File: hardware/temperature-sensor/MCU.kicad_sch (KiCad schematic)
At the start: 4 parts, among them U1 STM32F407V_E-G_Tx, Y1 CX2016FB25000C0FZZH1

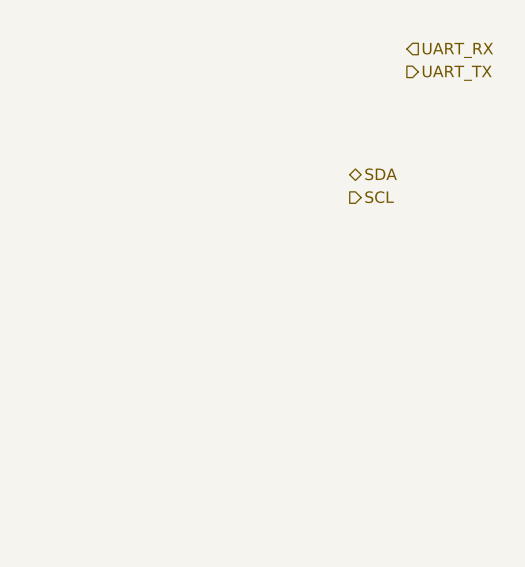
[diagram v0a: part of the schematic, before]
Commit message: add connection to FAN PWM and TACH
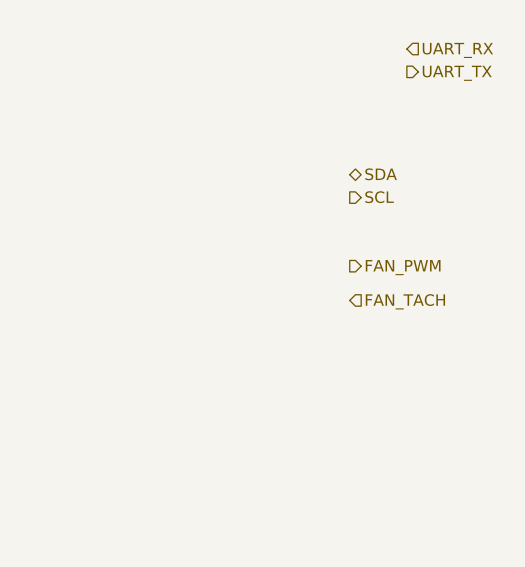
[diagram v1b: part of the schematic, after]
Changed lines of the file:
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@@
+		)
+	)
+	(hierarchical_label "FAN_PWM"
+		(shape output)
+		(at 224.79 114.3 0)
+		(effects
+			(font
+				(size 1.27 1.27)
+			)
+			(justify left)
 		)
 	)
@@
 		)
 	)
+	(hierarchical_label "FAN_TACH"
+		(shape input)
+		(at 224.79 118.11 0)
+		(effects
+			(font
+				(size 1.27 1.27)
+			)
+			(justify left)
+		)
+	)

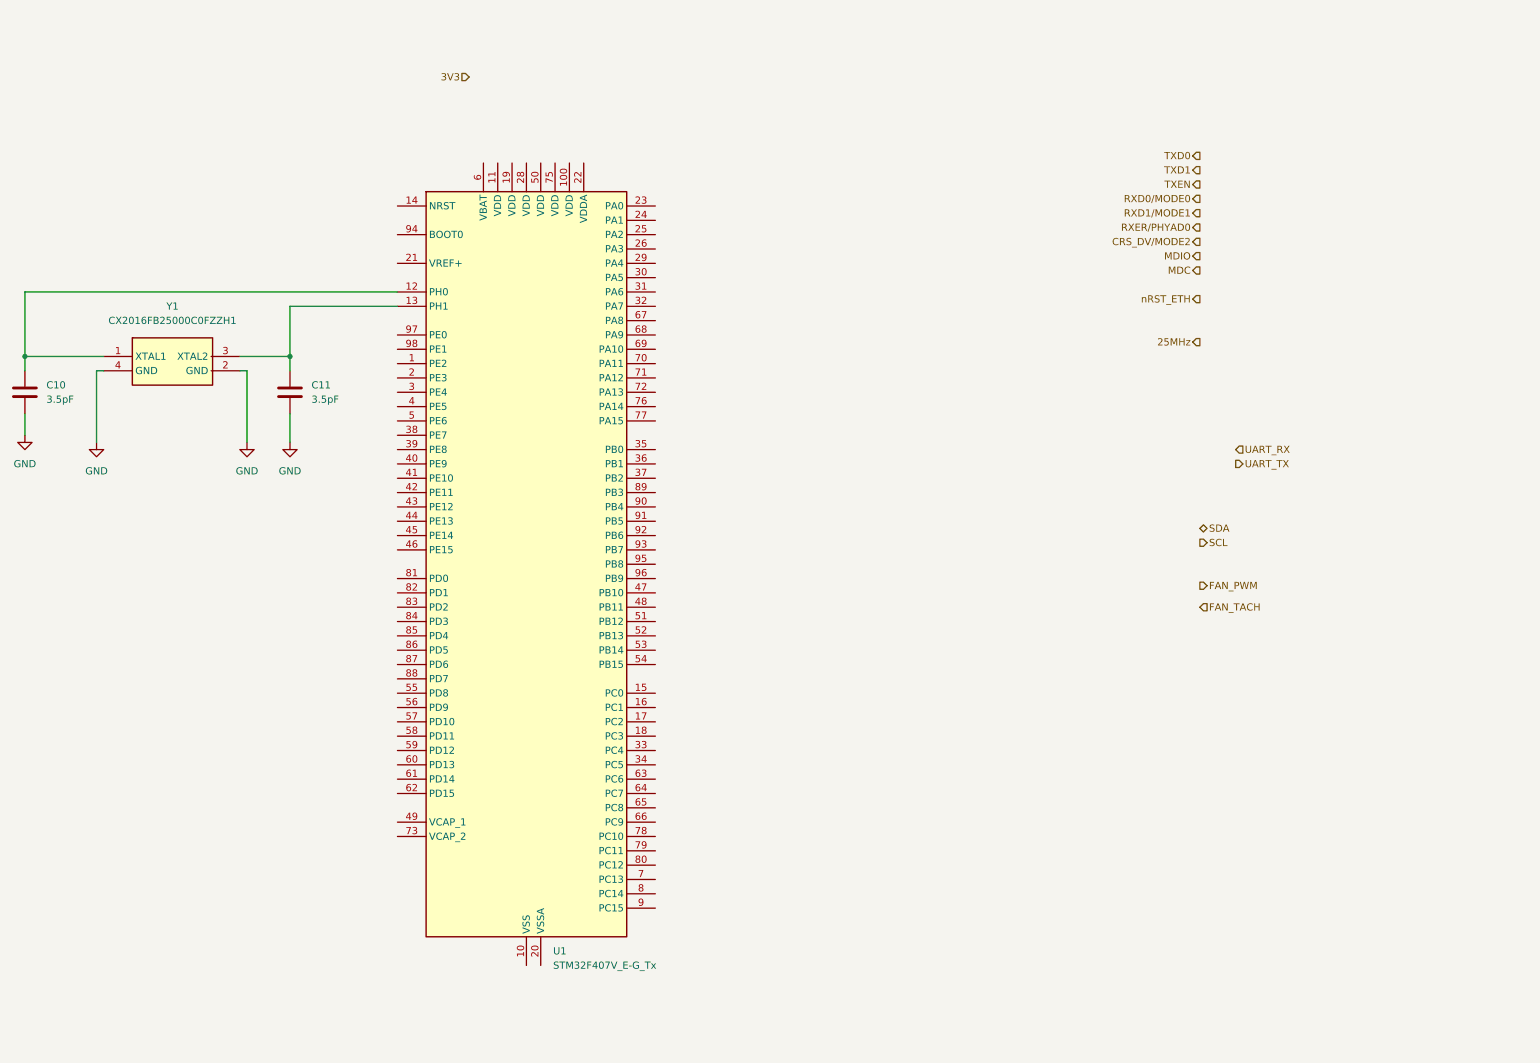
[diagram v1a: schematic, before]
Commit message: work on temperature sensor
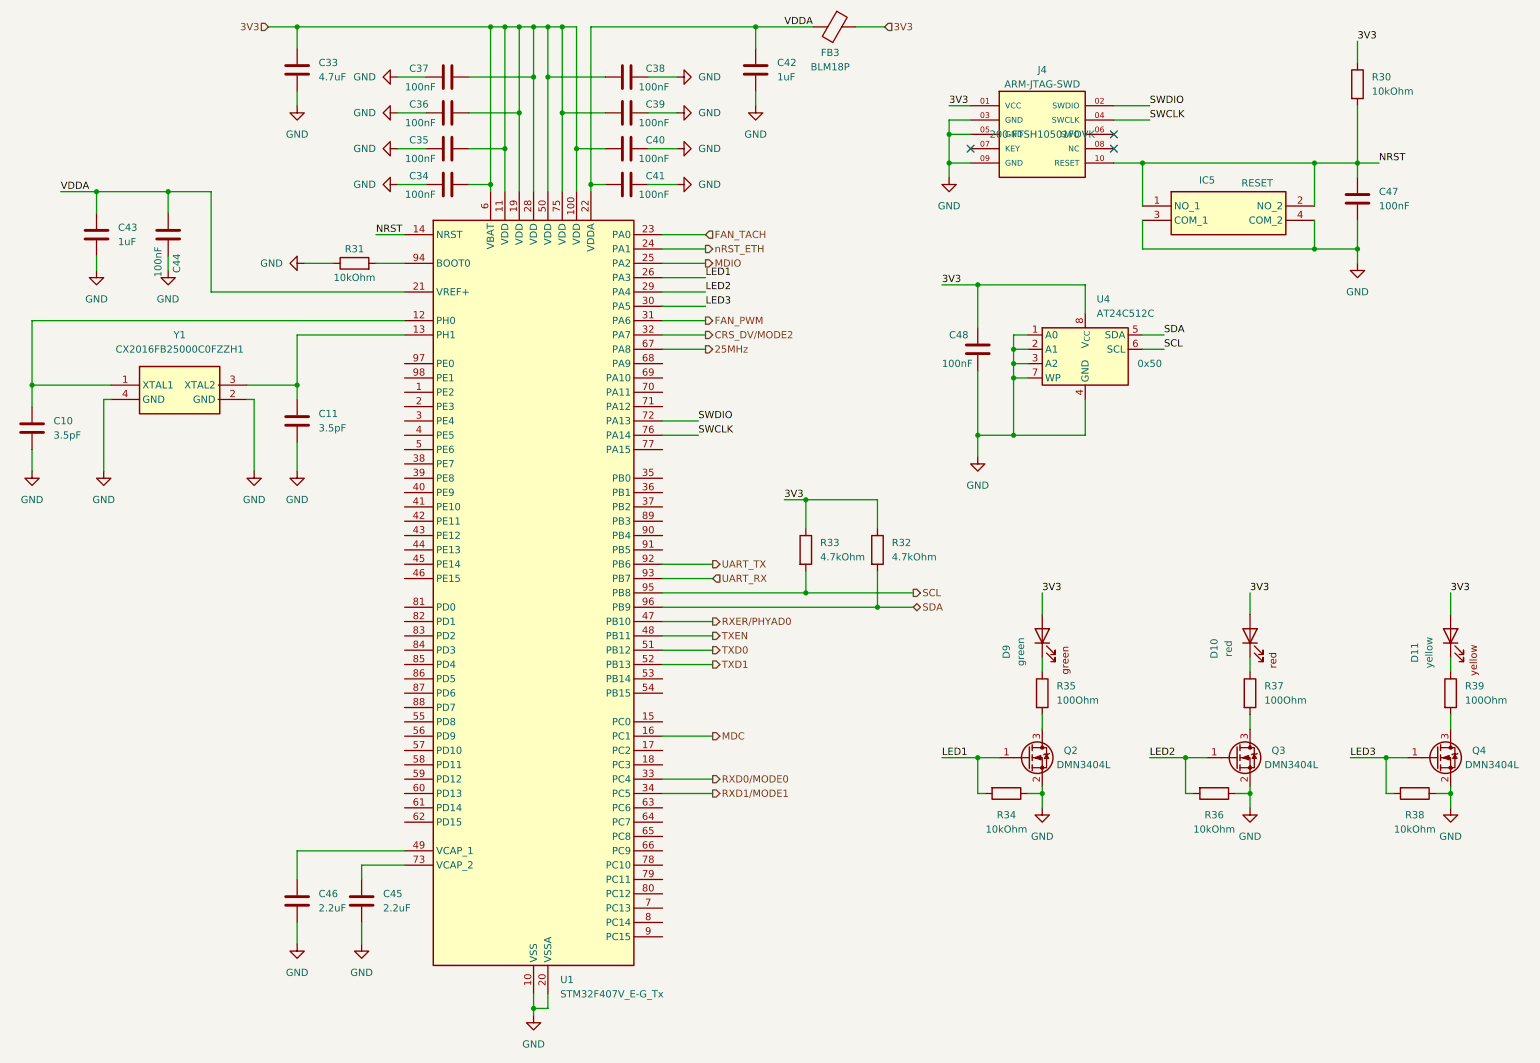
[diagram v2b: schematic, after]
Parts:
- added C33: 4.7uF, benediktibk:C_0805_2012Metric_Pad1.18x1.45mm_HandSolder, symbol benediktibk:C_4_7uF_SMD_0805_50V_10%
- added C34, C35, C36, C37, C38, C39, C40, C41, C44, C47, C48: 100nF, benediktibk:C_0603_1608Metric_Pad1.08x0.95mm_HandSolder, symbol benediktibk:C_100nF_SMD_0603_50V
- added C42, C43: 1uF, benediktibk:C_0603_1608Metric_Pad1.08x0.95mm_HandSolder, symbol benediktibk:C_1uF_SMD_0603_50V_10%
- added C45, C46: 2.2uF, benediktibk:C_0603_1608Metric_Pad1.08x0.95mm_HandSolder, symbol benediktibk:C_2_2uF_SMD_0603_10V_10%
- added D10: red, benediktibk:D_0603_1608Metric_Pad1.05x0.95mm_HandSolder, symbol benediktibk:LED_red_0603
- added D11: yellow, benediktibk:D_0603_1608Metric_Pad1.05x0.95mm_HandSolder, symbol benediktibk:LED_yellow_0603
- added D9: green, benediktibk:D_0603_1608Metric_Pad1.05x0.95mm_HandSolder, symbol benediktibk:LED_green_0603
- added FB3: BLM18P, benediktibk:R_0603_1608Metric_Pad0.98x0.95mm_HandSolder, symbol benediktibk:BLM18P
- added IC5: RESET, benediktibk:TS026650BK100SCRD, symbol benediktibk:TS02-66-50-BK-100-SCR-D
- added J4: ARM-JTAG-SWD, benediktibk:SAMTEC_FTSH-105-01-F-DV-P-TR, symbol benediktibk:ARM-JTAG-SWD
- added Q2, Q3, Q4: DMN3404L, benediktibk:SOT-23, symbol benediktibk:DMN3404L
- added R30, R31, R34, R36, R38: 10kOhm, benediktibk:R_0603_1608Metric_Pad0.98x0.95mm_HandSolder, symbol benediktibk:R_10kOhm_SMD_0603_100mW_1%
- added R32, R33: 4.7kOhm, benediktibk:R_0603_1608Metric_Pad0.98x0.95mm_HandSolder, symbol benediktibk:R_4_7kOhm_SMD_0603_100mW_1%
- added R35, R37, R39: 100Ohm, benediktibk:R_0603_1608Metric_Pad0.98x0.95mm_HandSolder, symbol benediktibk:R_100Ohm_SMD_0603_100mW_1%
- added U4: AT24C512C, benediktibk:SOIC127P600X175-8N, symbol benediktibk:AT24C512C
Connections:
- net 25MHz: now also U1.67 (PA8)
- net 3V3: now also U1.100 (VDD), U1.11 (VDD), U1.19 (VDD), U1.28 (VDD), U1.50 (VDD), U1.6 (VBAT), U1.75 (VDD), C33.1, C34.1, C35.1, C36.1, C37.1, C38.1, C39.1, C40.1, C48.1, D10.2 (A), D11.2 (A), D9.2 (A), FB3.1, J4.01 (VCC), R30.1, R32.1, R33.1, U4.8 (V_{CC})
- net CRS_DV/MODE2: now also U1.32 (PA7)
- net FAN_PWM: now also U1.31 (PA6)
- net FAN_TACH: now also U1.23 (PA0)
- net GND: now also U1.10 (VSS), U1.20 (VSSA), U1.27 (VSS), U1.74 (VSS), U1.99 (VSS), C33.2, C34.2, C35.2, C36.2, C37.2, C38.2, C39.2, C40.2, C41.2, C42.2, C43.2, C44.2, C45.2, C46.2, C47.2, C48.2, IC5.3 (COM_1), IC5.4 (COM_2), J4.03 (GND), J4.05 (GND), J4.09 (GND), Q2.2 (S), Q3.2 (S), Q4.2 (S), R31.1, R34.1, R36.1, R38.1, U4.1 (A0), U4.2 (A1), U4.3 (A2), U4.4 (GND), U4.7 (WP)
- net MDC: now also U1.16 (PC1)
- net MDIO: now also U1.25 (PA2)
- net RXD0/MODE0: now also U1.33 (PC4)
- net RXD1/MODE1: now also U1.34 (PC5)
- net RXER/PHYAD0: now also U1.47 (PB10)
- net SCL: now also U1.95 (PB8), R33.2, U4.6 (SCL)
- net SDA: now also U1.96 (PB9), R32.2, U4.5 (SDA)
- net TXD0: now also U1.51 (PB12)
- net TXD1: now also U1.52 (PB13)
- net TXEN: now also U1.48 (PB11)
- net UART_RX: now also U1.93 (PB7)
- net UART_TX: now also U1.92 (PB6)
- net nRST_ETH: now also U1.24 (PA1)
- net NRST: now reaches U1.14 (NRST)
- net NRST: now also C47.1, IC5.1 (NO_1), IC5.2 (NO_2), J4.10 (RESET), R30.2
- net VDDA: now reaches U1.21 (VREF+)
- net VDDA: now also U1.22 (VDDA), C41.1, C42.1, C43.1, C44.1, FB3.2
- net LED1: now reaches U1.26 (PA3)
- net LED1: now also Q2.1 (G), R34.2
- net LED2: now reaches U1.29 (PA4)
- net LED2: now also Q3.1 (G), R36.2
- net LED3: now reaches U1.30 (PA5)
- net LED3: now also Q4.1 (G), R38.2
- net at U1.49 (VCAP_1): now also C46.1
- net SWDIO: now reaches U1.72 (PA13)
- net SWDIO: now also J4.02 (SWDIO)
- net at U1.73 (VCAP_2): now also C45.1
- net SWCLK: now reaches U1.76 (PA14)
- net SWCLK: now also J4.04 (SWCLK)
- net at U1.94 (BOOT0): now also R31.2
- new net: D10.1 (K), R37.1
- new net: Q3.3 (D), R37.2
- new net: D11.1 (K), R39.1
- new net: Q2.3 (D), R35.2
- new net: Q4.3 (D), R39.2
- new net: D9.1 (K), R35.1
- no-connect marks 0 -> 3
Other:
- moved on the sheet: C10, C11, U1, Y1

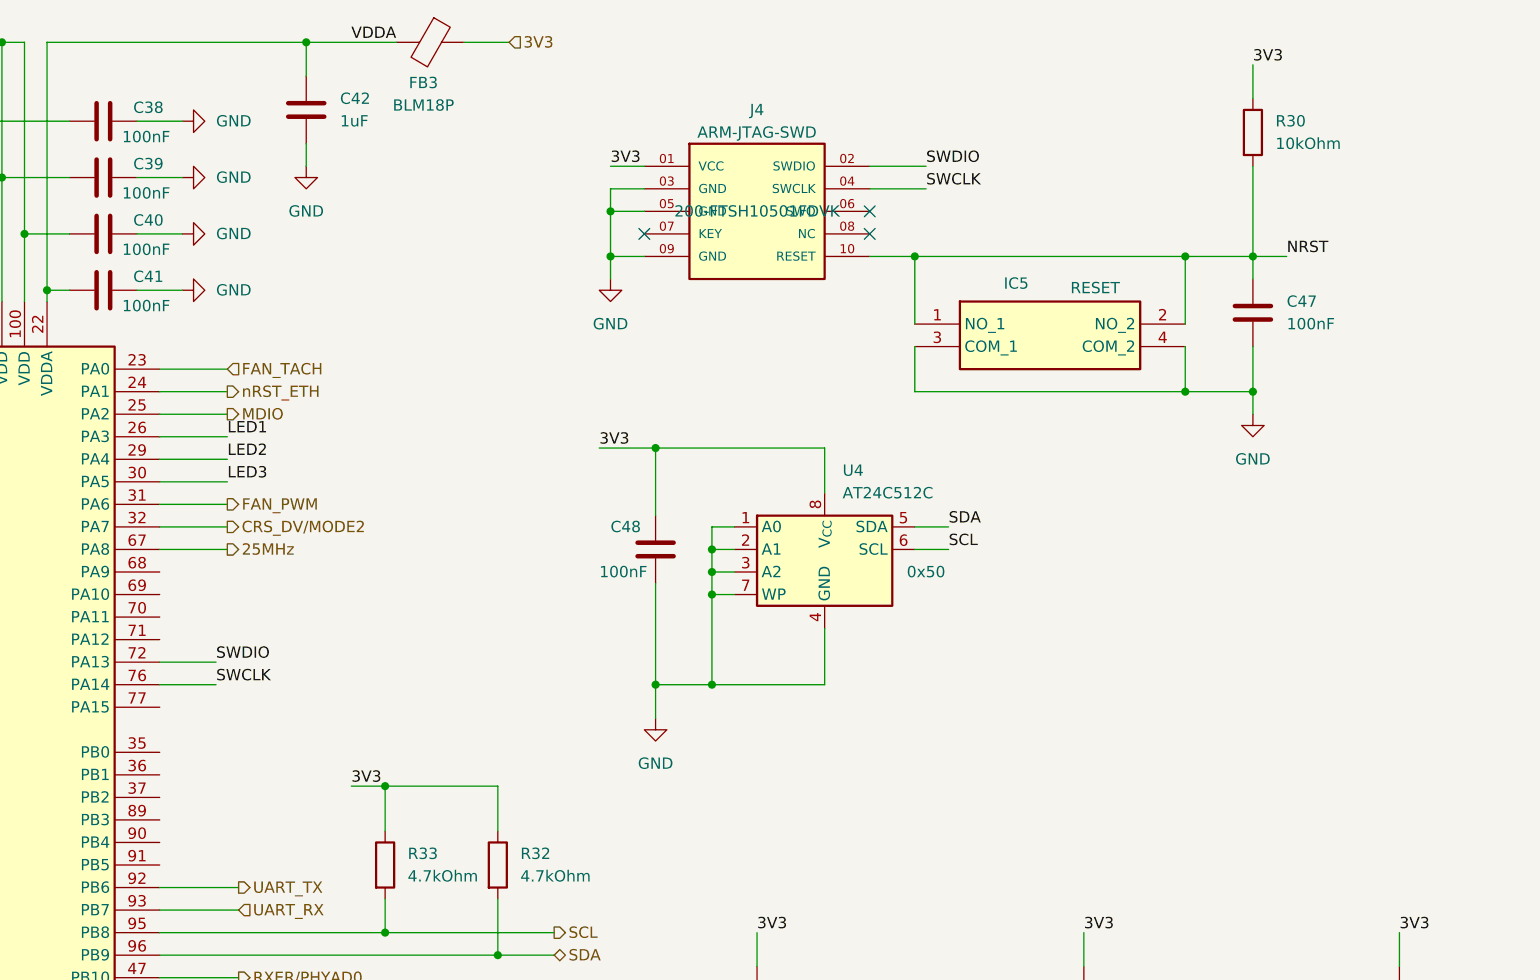
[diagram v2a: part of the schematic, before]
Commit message: place components of PoE
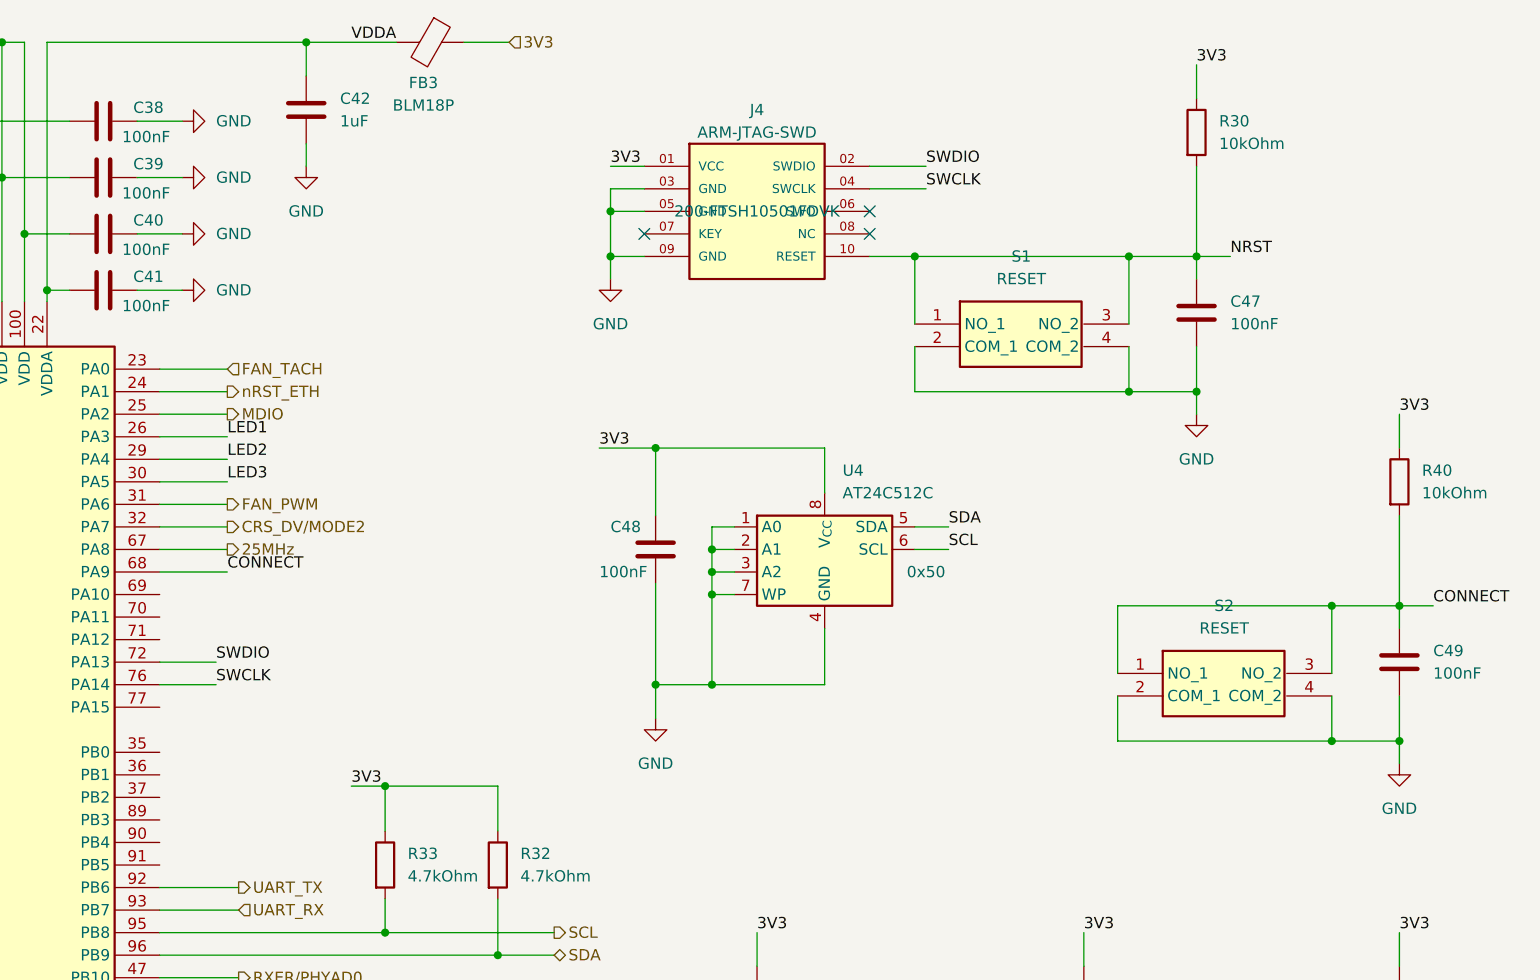
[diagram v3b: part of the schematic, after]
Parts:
- removed IC5: RESET, benediktibk:TS026650BK100SCRD, symbol benediktibk:TS02-66-50-BK-100-SCR-D
- added C49: 100nF, benediktibk:C_0603_1608Metric_Pad1.08x0.95mm_HandSolder, symbol benediktibk:C_100nF_SMD_0603_50V
- added R40: 10kOhm, benediktibk:R_0603_1608Metric_Pad0.98x0.95mm_HandSolder, symbol benediktibk:R_10kOhm_SMD_0603_100mW_1%
- added S1, S2: RESET, benediktibk:TS046673BK100SMT, symbol benediktibk:TS04-66-73-BK-100-SMT
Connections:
- net 3V3: now also R40.1
- net GND: now also C49.2, S1.2 (COM_1), S1.4 (COM_2), S2.2 (COM_1), S2.4 (COM_2)
- net NRST: now also S1.1 (NO_1), S1.3 (NO_2)
- net CONNECT: now reaches U1.68 (PA9)
- net CONNECT: now also C49.1, R40.2, S2.1 (NO_1), S2.3 (NO_2)
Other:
- moved on the sheet: C47, R30
